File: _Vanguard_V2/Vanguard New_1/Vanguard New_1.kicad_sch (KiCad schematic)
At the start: 9 parts, among them J1 USB_B_Micro, J2 Conn_01x03_Pin, J3 Screw_Terminal_01x02, Q1 IRLB8721PBF, U1 ATSAMD11D14A-M, U2 BNO055, U3 ATSAMD21G18A-A, U4 BMP280

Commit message: added flash card to schematic
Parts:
- added J4: Micro_SD_Card, symbol Connector:Micro_SD_Card
- added U5: W25Q32JVZPIQ, W25Q32JVZPIQ:SON127P600X500X80-9N, symbol W25Q32JVZPIQ:W25Q32JVZPIQ

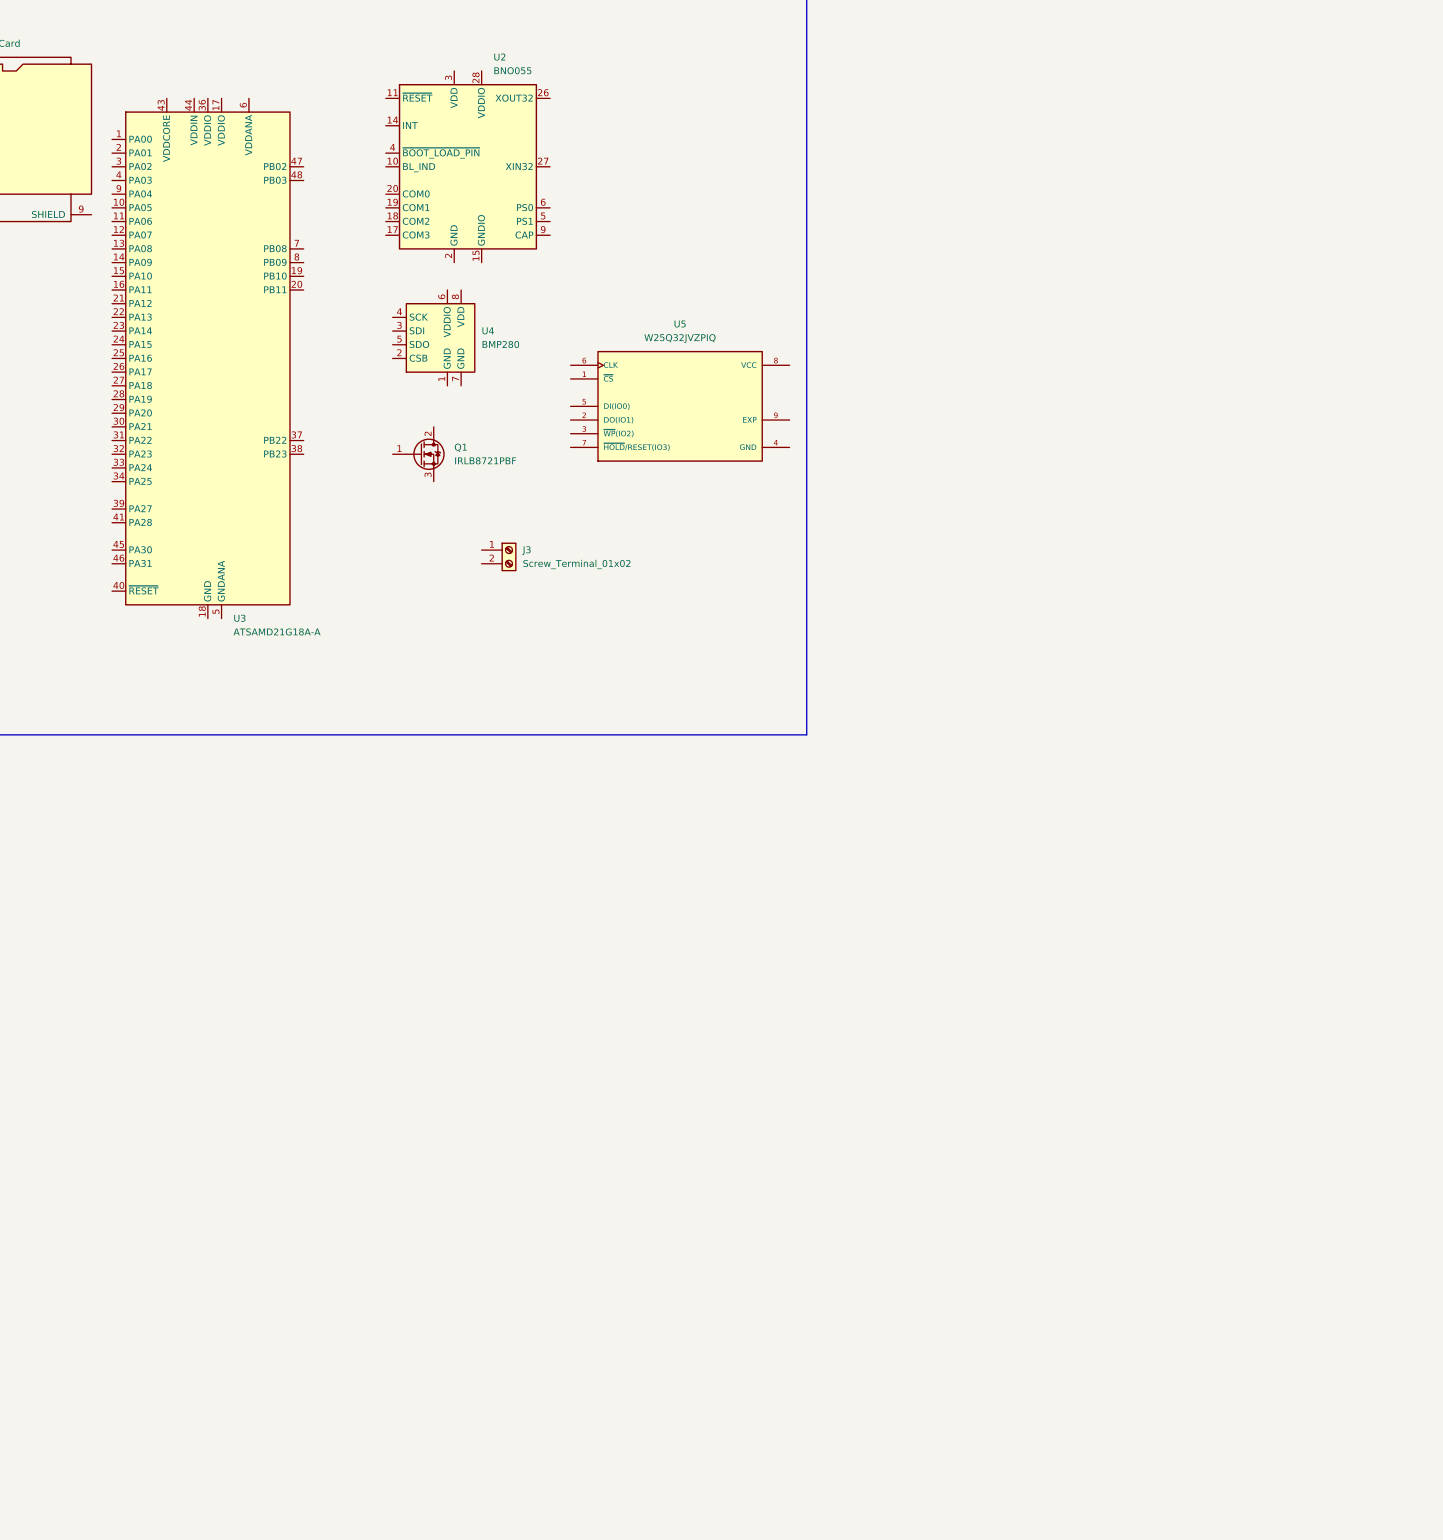
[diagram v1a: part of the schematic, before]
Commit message: new mcu
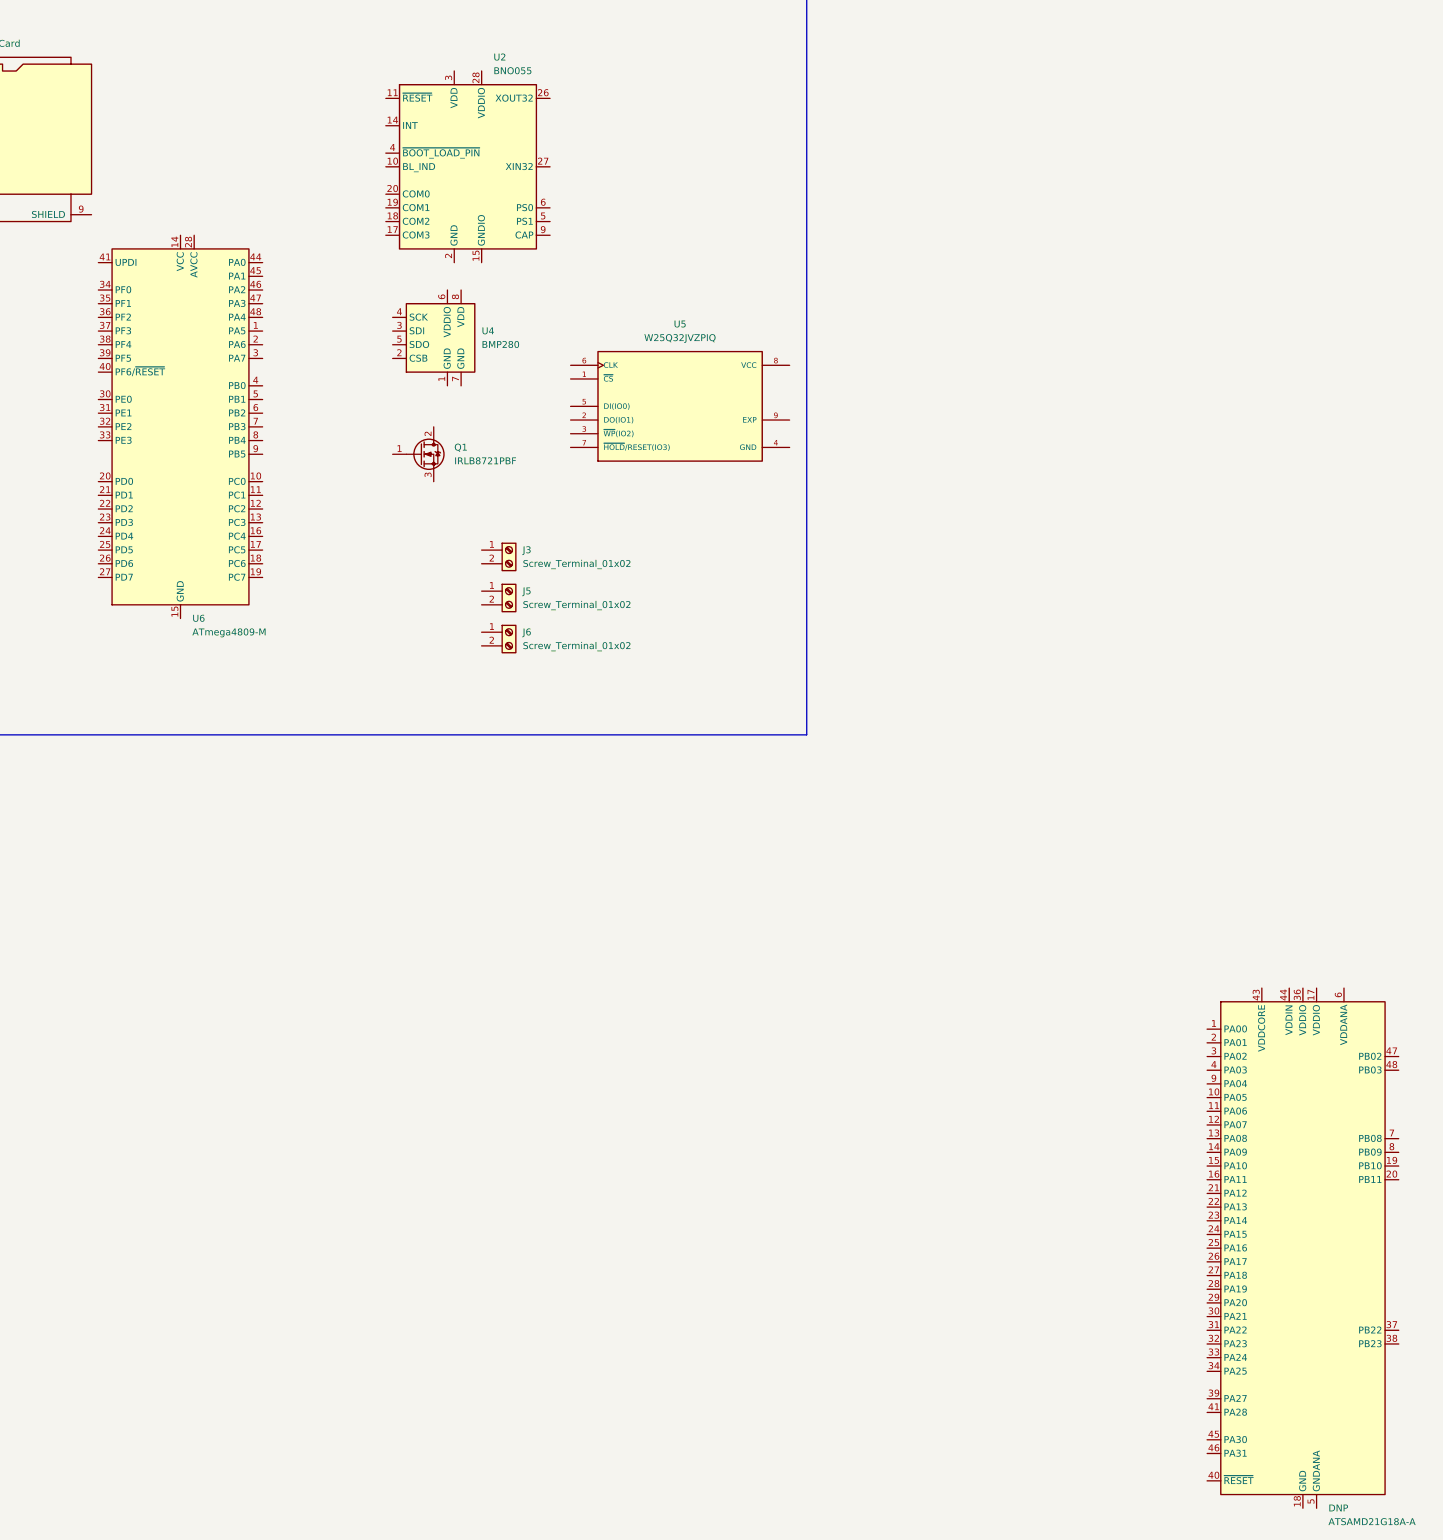
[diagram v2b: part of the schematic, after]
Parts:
- added J5, J6: Screw_Terminal_01x02, symbol Connector:Screw_Terminal_01x02
- added U6: ATmega4809-M, Package_DFN_QFN:UQFN-48-1EP_6x6mm_P0.4mm_EP4.62x4.62mm, symbol MCU_Microchip_ATmega:ATmega4809-M
- renumbered U3 to DNP
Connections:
- new net: U6.14 (VCC), U6.42 (VCC)
- new net: U6.15 (GND), U6.29 (GND), U6.43 (GND), U6.49 (GND)
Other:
- moved on the sheet: DNP

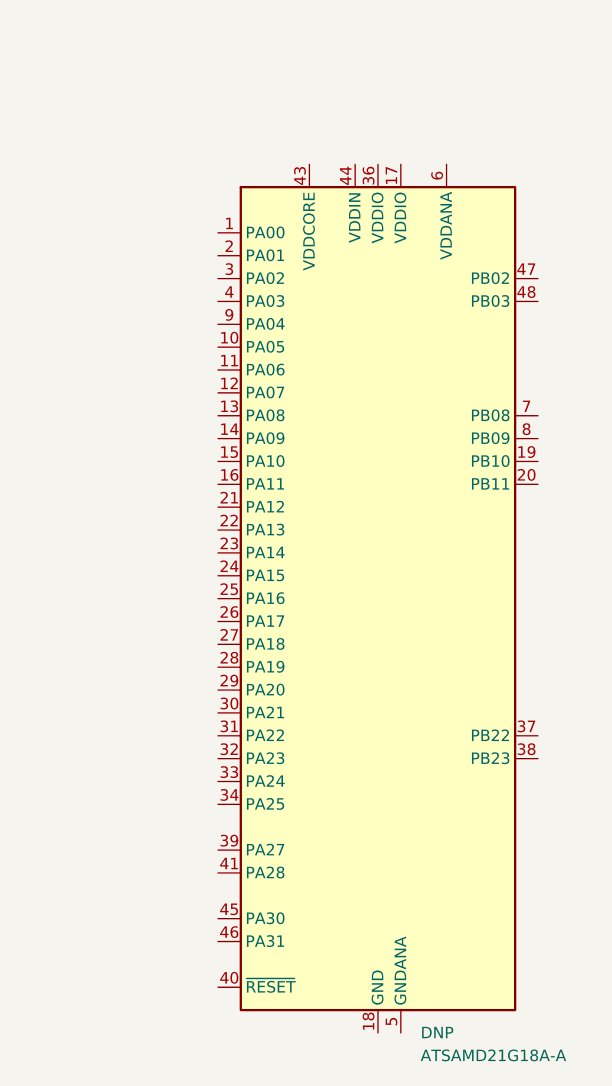
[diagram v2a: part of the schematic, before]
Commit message: noticed old mcu not deleted
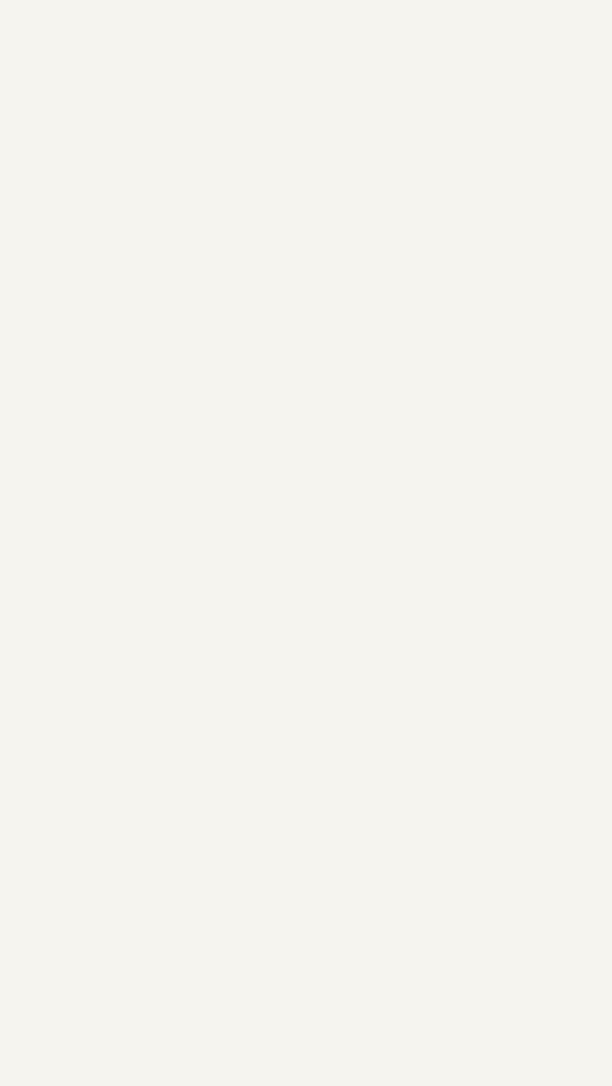
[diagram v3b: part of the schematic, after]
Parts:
- removed DNP: ATSAMD21G18A-A, Package_QFP:TQFP-48_7x7mm_P0.5mm, symbol MCU_Microchip_SAMD:ATSAMD21G18A-A
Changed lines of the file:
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@@
-	)
-	(symbol
-		(lib_id "MCU_Microchip_SAMD:ATSAMD21G18A-A")
-		(at 505.46 327.66 0)
-		(unit 1)
-		(exclude_from_sim no)
-		(in_bom yes)
-		(on_board yes)
-		(dnp no)
-		(fields_autoplaced yes)
-		(property "Reference" "DNP"
-			(at 510.1941 375.92 0)
-			(effects
-				(font
-					(size 1.27 1.27)
-				)
-				(justify left)
-			)
-		)
-		(property "Value" "ATSAMD21G18A-A"
-			(at 510.1941 378.46 0)
-			(effects
-				(font
-					(size 1.27 1.27)
-				)
-				(justify left)
-			)
-		)
-		(property "Footprint" "Package_QFP:TQFP-48_7x7mm_P0.5mm"
-			(at 528.32 374.65 0)
-			(effects
-				(font
-					(size 1.27 1.27)
-				)
-				(hide yes)
-			)
-		)
-		(property "Datasheet" "http://ww1.microchip.com/downloads/en/DeviceDoc/SAM_D21_DA1_Family_Data%20Sheet_DS40001882E.pdf"
-			(at 505.46 302.26 0)
-			(effects
-				(font
-					(size 1.27 1.27)
-				)
-				(hide yes)
-			)
-		)
-		(property "Description" "SAM D21 Microchip SMART ARM-based Flash MCU, 48Mhz, 256K Flash, 32K SRAM, TQFP-48"
-			(at 505.46 327.66 0)
-			(effects
-				(font
-					(size 1.27 1.27)
-				)
-				(hide yes)
-			)
-		)
-		(pin "19"
-		)
-		(pin "1"
-		)
-		(pin "25"
-		)
-		(pin "15"
-		)
-		(pin "16"
-		)
-		(pin "17"
-		)
-		(pin "18"
-		)
-		(pin "11"
-		)
-		(pin "8"
-		)
-		(pin "9"
-		)
-		(pin "10"
-		)
-		(pin "2"
-		)
-		(pin "12"
-		)
-		(pin "33"
-		)
-		(pin "42"
-		)
-		(pin "4"
-		)
-		(pin "43"
-		)
-		(pin "27"
-		)
-		(pin "21"
-		)
-		(pin "26"
-		)
-		(pin "6"
-		)
-		(pin "7"
-		)
-		(pin "31"
-		)
-		(pin "29"
-		)
-		(pin "3"
-		)
-		(pin "22"
-		)
-		(pin "32"
-		)
-		(pin "30"
-		)
-		(pin "28"
-		)
-		(pin "20"
-		)
-		(pin "46"
-		)
-		(pin "47"
-		)
-		(pin "41"
-		)
-		(pin "40"
-		)
-		(pin "36"
-		)
-		(pin "44"
-		)
-		(pin "14"
-		)
-		(pin "13"
-		)
-		(pin "34"
-		)
-		(pin "35"
-		)
-		(pin "39"
-		)
-		(pin "37"
-		)
-		(pin "23"
-		)
-		(pin "24"
-		)
-		(pin "45"
-		)
-		(pin "48"
-		)
-		(pin "5"
-		)
-		(pin "38"
-		)
-		(instances
-			(project ""
-				(path "/3bcd31b7-c263-4dfd-992b-897acec3941c"
-					(reference "DNP")
-					(unit 1)
-				)
-			)
-		)
 	)
 	(symbol
